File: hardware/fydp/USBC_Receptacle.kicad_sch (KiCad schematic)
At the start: 6 parts, among them J1 1054500101, J2 Conn_01x02_Pin, J22 Barrel_Jack

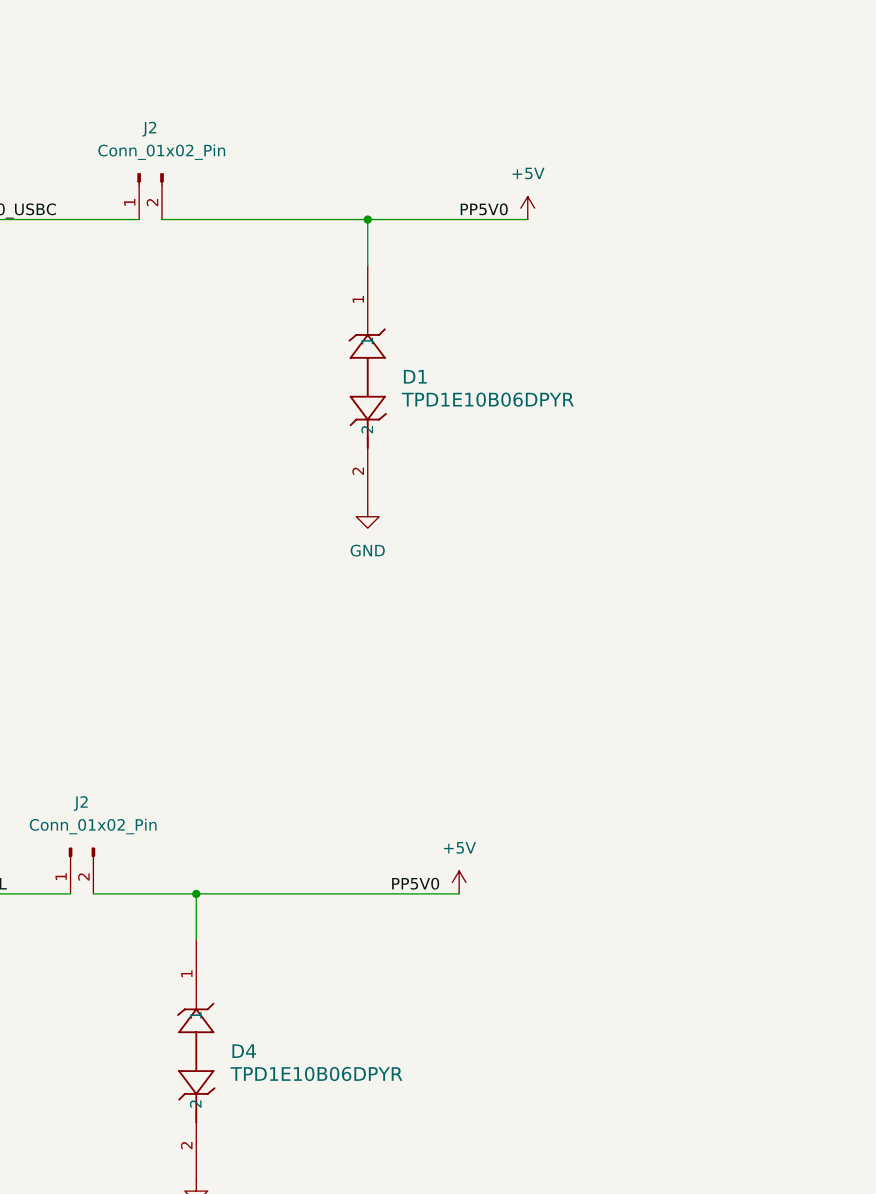
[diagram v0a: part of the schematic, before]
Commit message: Remove 2 channels of multiplier and change ADC
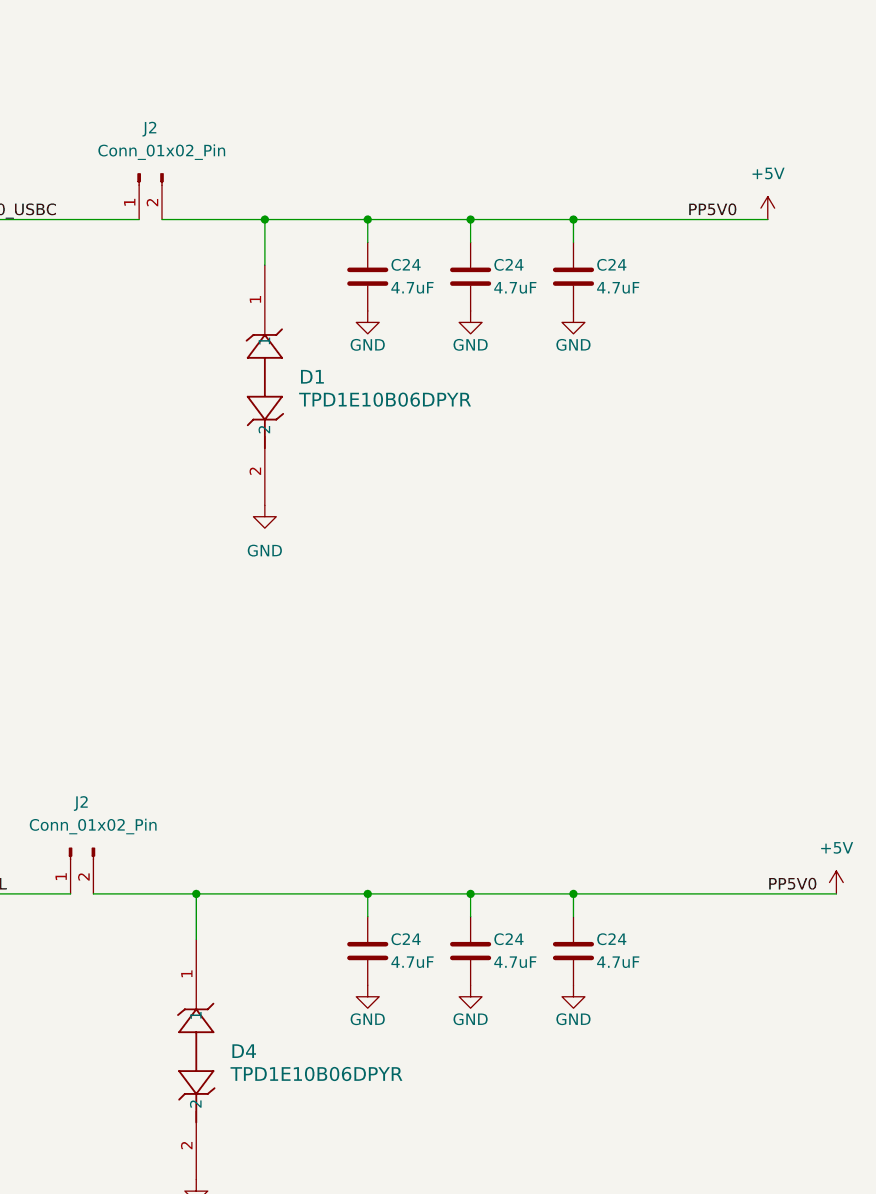
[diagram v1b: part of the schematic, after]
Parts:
- added C24 (x6): 4.7uF, Capacitor_SMD:C_0805_2012Metric, symbol Device:C
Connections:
- net +5V: now also C24.1, C24.1, C24.1, C24.1, C24.1, C24.1
- net GND: now also C24.2, C24.2, C24.2, C24.2, C24.2, C24.2
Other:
- moved on the sheet: D1

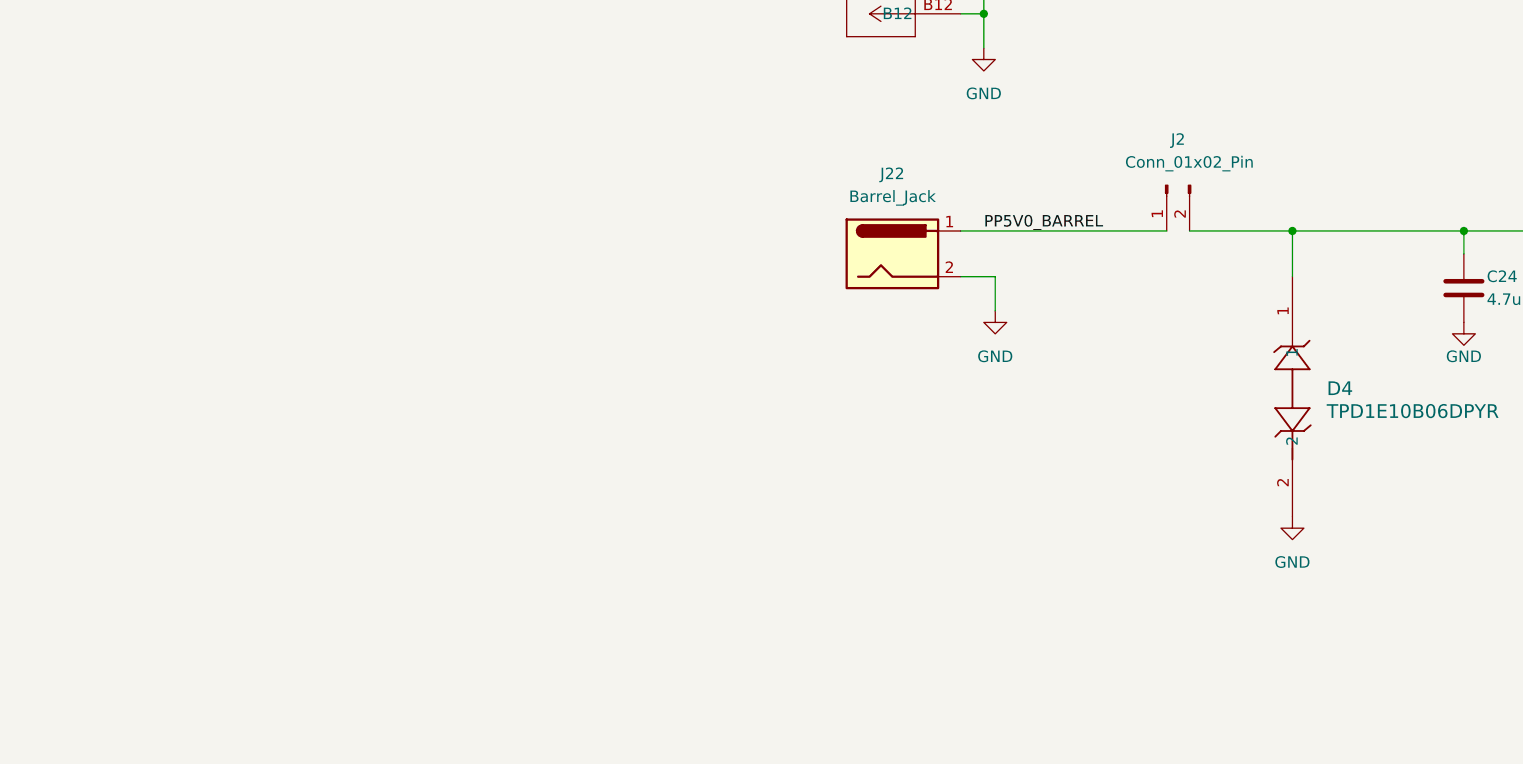
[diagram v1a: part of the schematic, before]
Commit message: Completed placement and silk for left and centre sections of the PCB
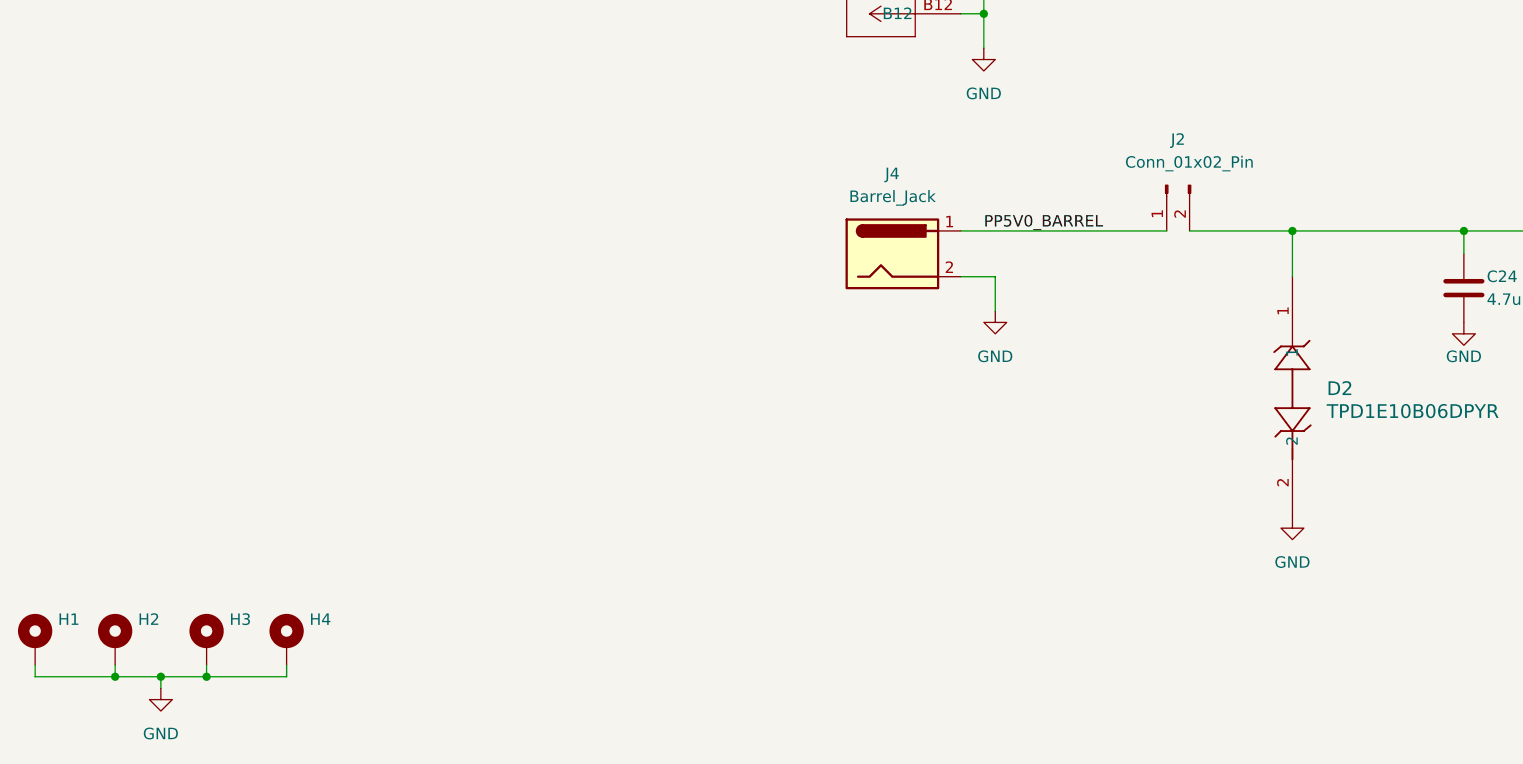
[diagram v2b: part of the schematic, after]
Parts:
- added H1, H2, H3, H4: MountingHole_Pad, MountingHole:MountingHole_2.2mm_M2_Pad_TopBottom, symbol Mechanical:MountingHole_Pad
- renumbered D4 to D2, J22 to J4
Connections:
- net GND: now also H1.1, H2.1, H3.1, H4.1

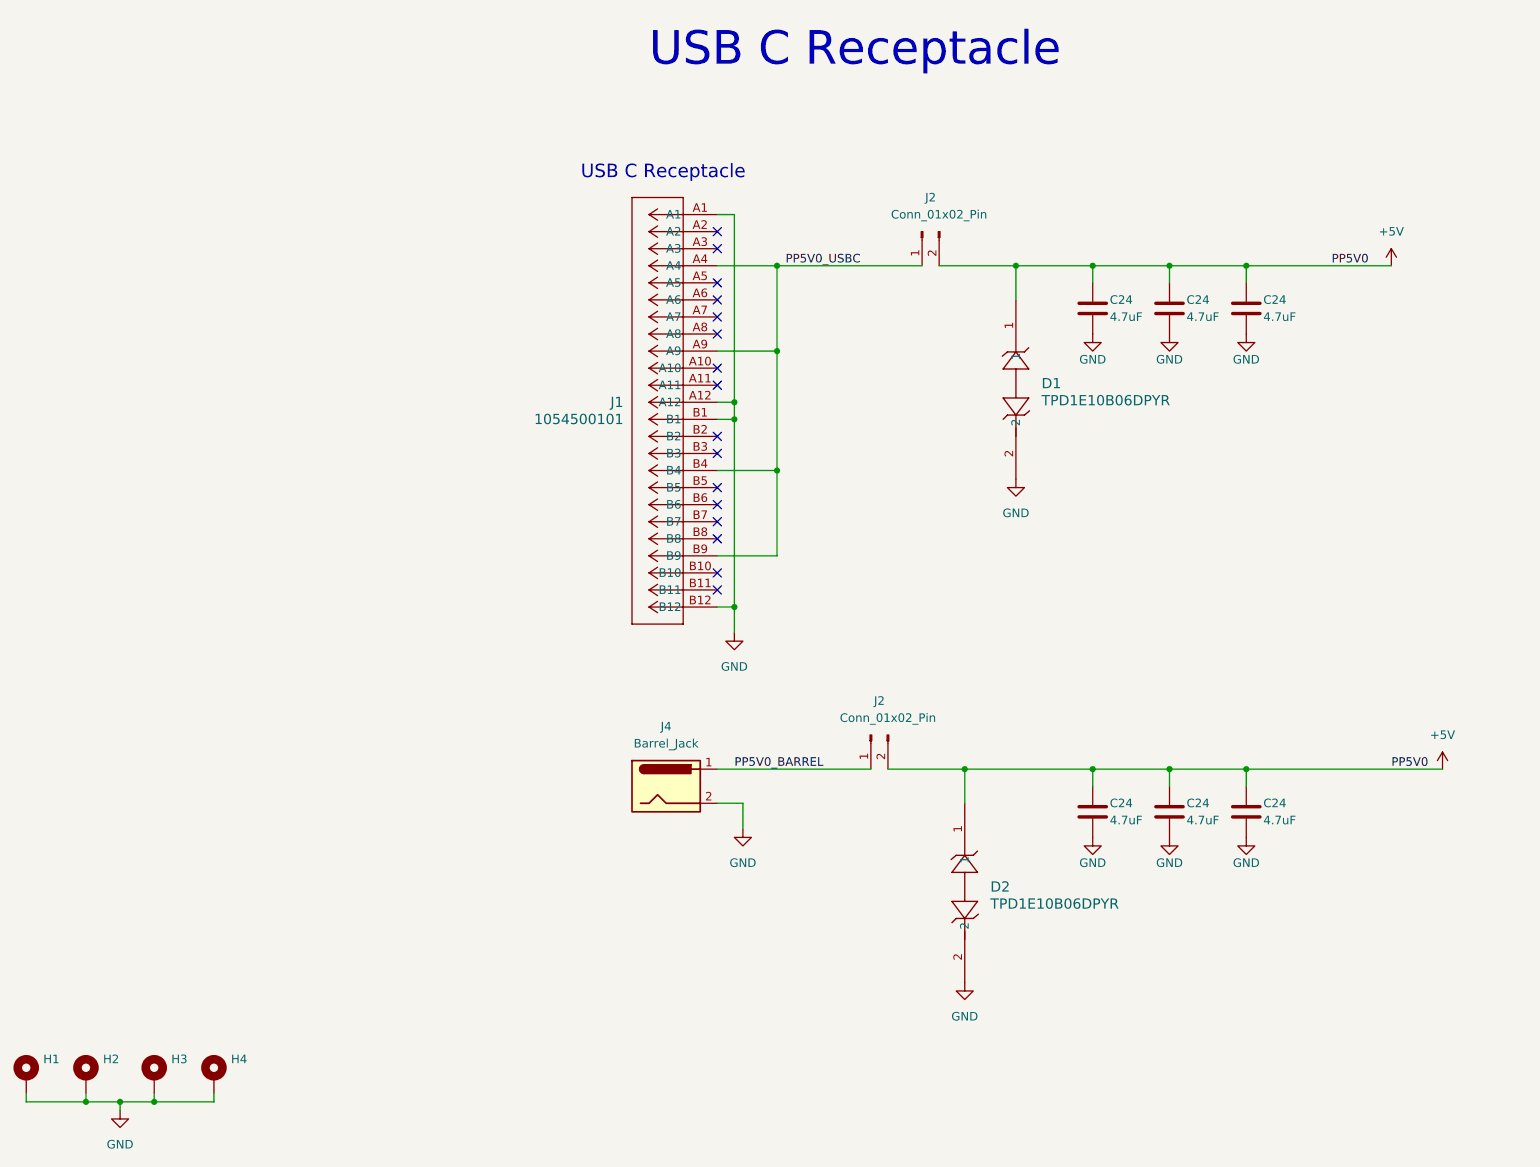
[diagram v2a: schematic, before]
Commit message: Initial layout is pretty much complete, need to add power planes
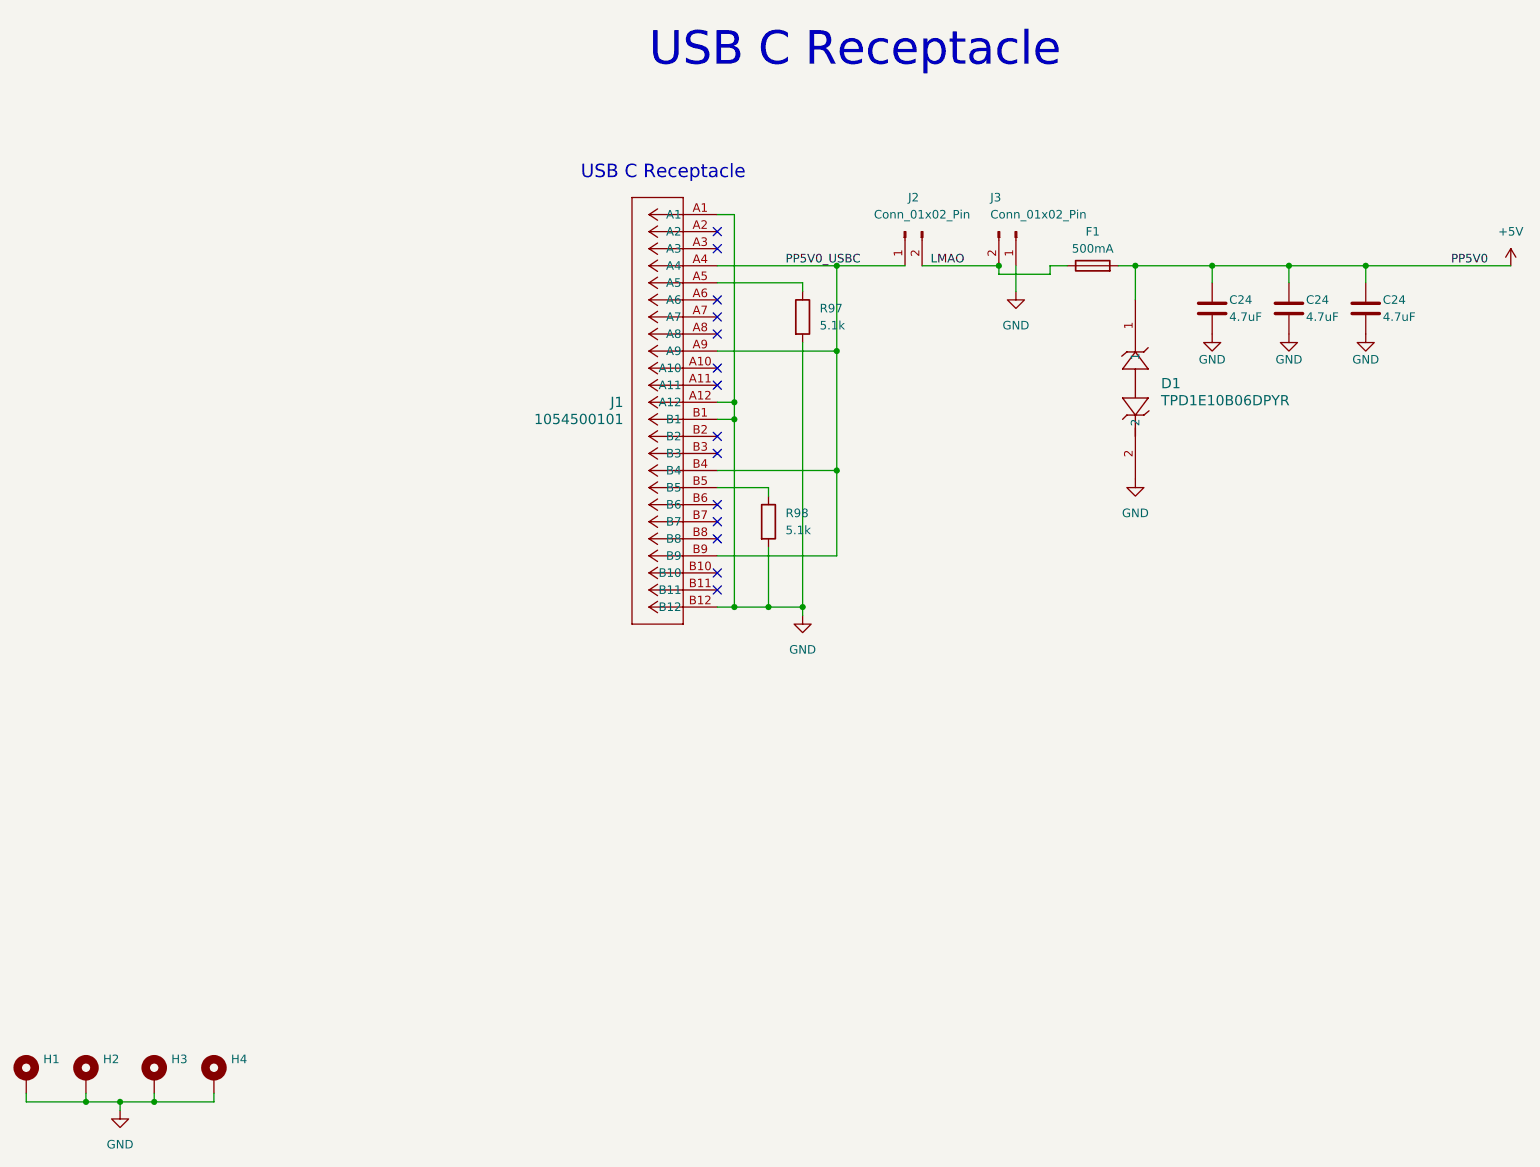
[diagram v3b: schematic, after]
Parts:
- removed C24 (x3): 4.7uF, Capacitor_SMD:C_0805_2012Metric, symbol Device:C
- removed D2: TPD1E10B06DPYR, Resistor_SMD:R_0402_1005Metric, symbol TPD1E10B06DPYR:TPD1E10B06DPYR
- removed J2: Conn_01x02_Pin, Connector_PinHeader_2.54mm:PinHeader_1x02_P2.54mm_Vertical, symbol Connector:Conn_01x02_Pin
- removed J4: Barrel_Jack, symbol Connector:Barrel_Jack
- added F1: 500mA, Fuse:Fuse_1206_3216Metric_Pad1.42x1.75mm_HandSolder, symbol Device:Fuse
- added J3: Conn_01x02_Pin, TerminalBlock_Phoenix:TerminalBlock_Phoenix_PT-1,5-2-3.5-H_1x02_P3.50mm_Horizontal, symbol Connector:Conn_01x02_Pin
- added R97, R98: 5.1k, Resistor_SMD:R_0805_2012Metric, symbol Device:R
- D1: footprint Resistor_SMD:R_0402_1005Metric -> Resistor_SMD:R_0805_2012Metric
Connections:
- net +5V: now also F1.2; no longer J2.2 (Pin_2)
- net GND: now also J3.1 (Pin_1), R97.2, R98.2
- net at J1.A5: now also R97.1
- net at J1.B5: now also R98.1
- new net LMAO: F1.1, J2.2 (Pin_2), J3.2 (Pin_2)
- no-connect marks 16 -> 14
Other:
- moved on the sheet: C24, D1, J2
